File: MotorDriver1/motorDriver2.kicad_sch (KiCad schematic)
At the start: 24 parts, among them Q2 IRLZ44NSTRLPBF, Q3 IRLZ44NSTRLPBF, Q4 IRLZ44NSTRLPBF, Q5 IRLZ44NSTRLPBF

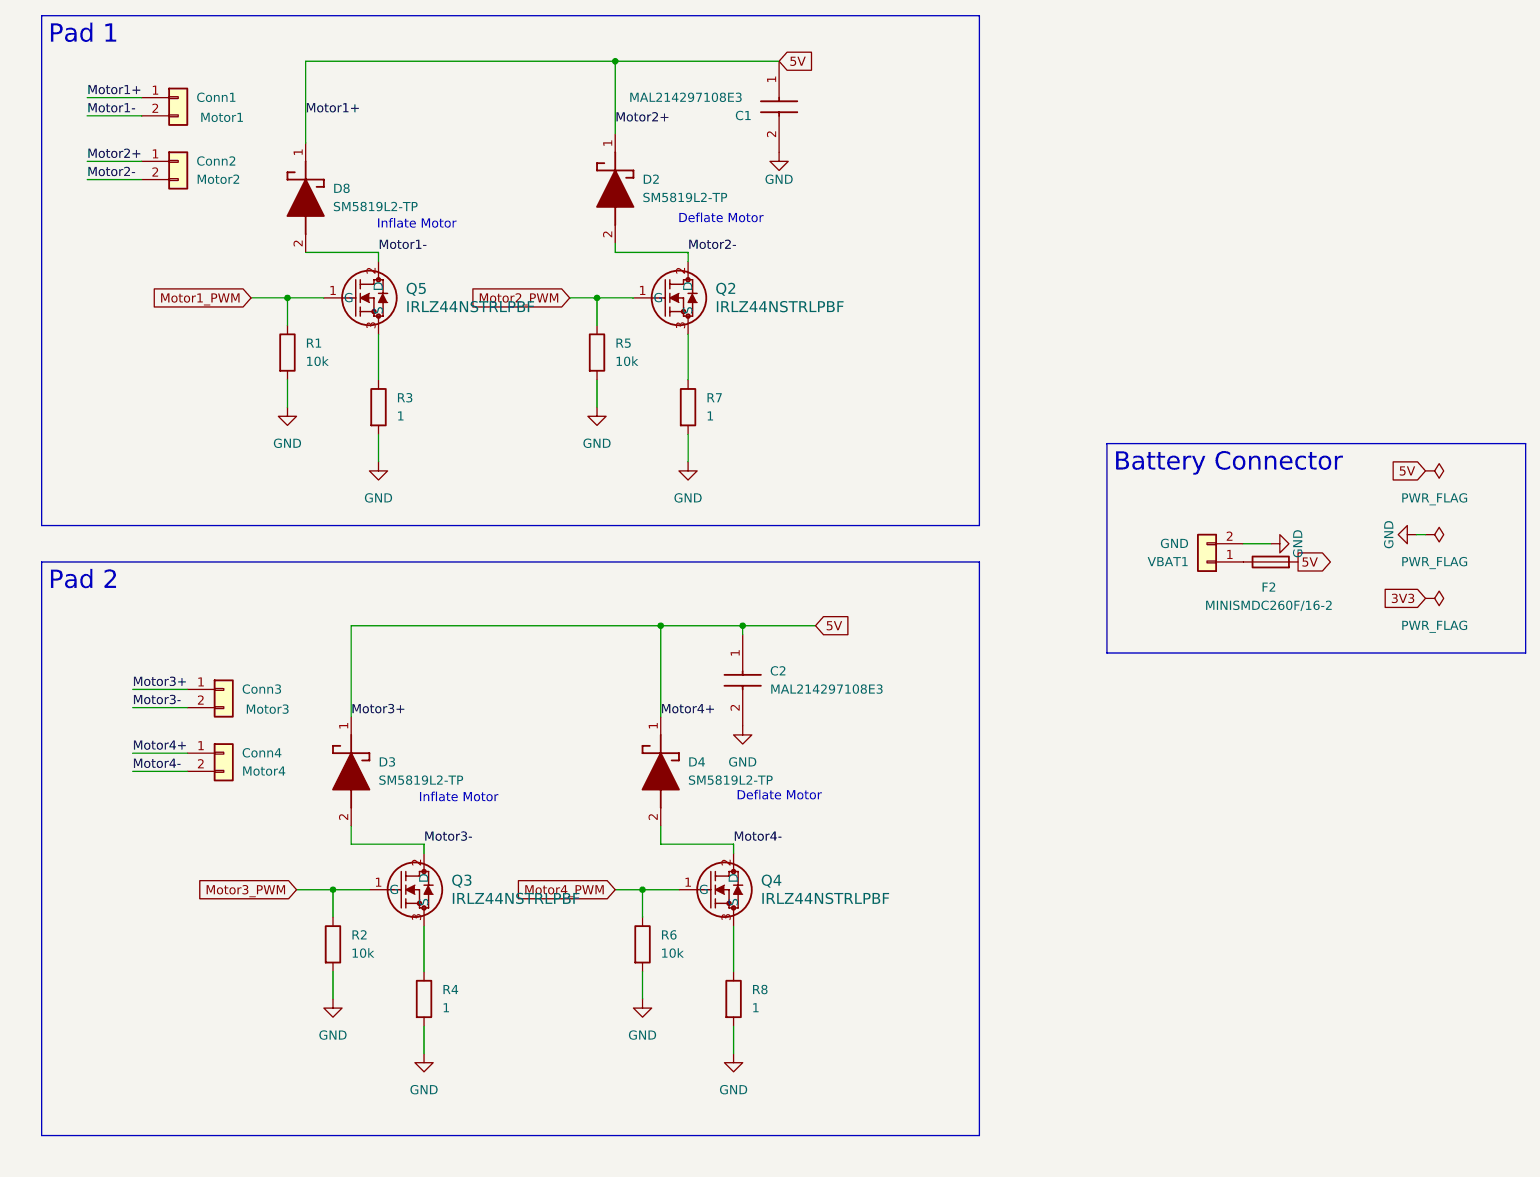
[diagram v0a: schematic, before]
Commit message: added motors and sensors for 4 pad system
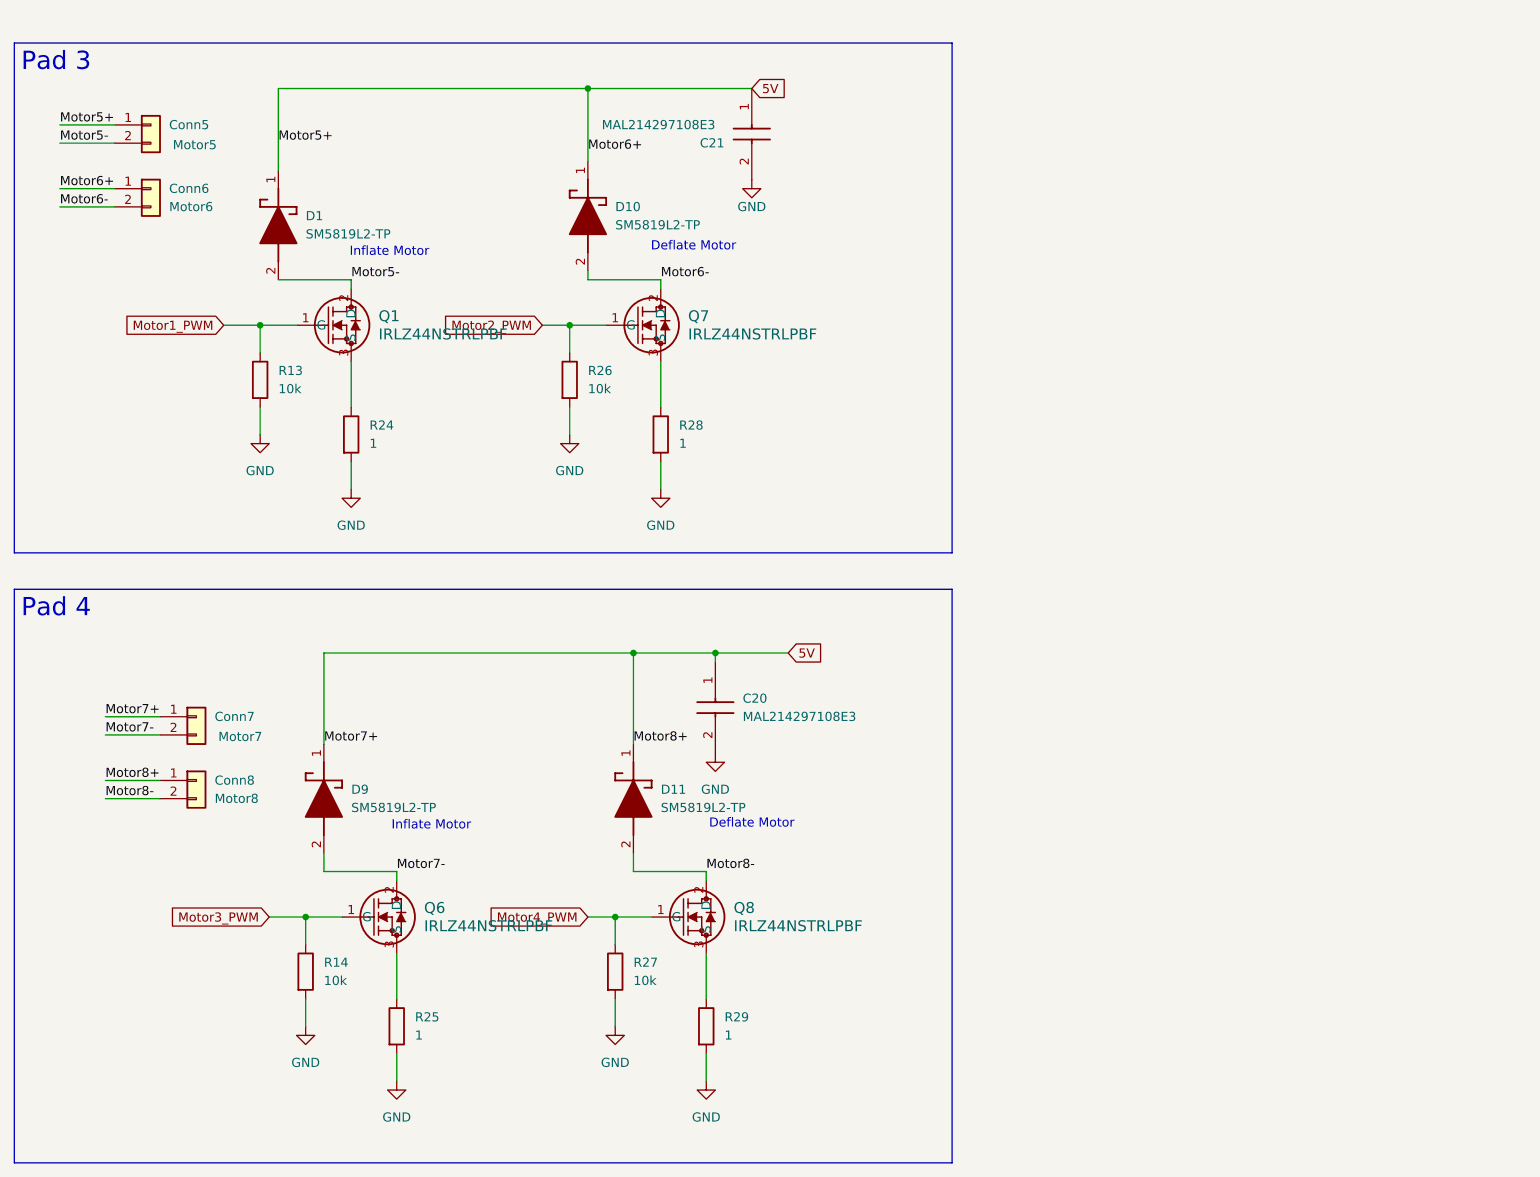
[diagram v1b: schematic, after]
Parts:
- removed C1, C2: MAL214297108E3, footprintLib:CAPAE680X800N, symbol pcb:MAL214297108E3
- removed Conn1: Motor1, Connector_PinHeader_2.54mm:PinHeader_1x02_P2.54mm_Vertical, symbol Connector_Generic:Conn_01x02
- removed Conn2: Motor2, Connector_PinHeader_2.54mm:PinHeader_1x02_P2.54mm_Vertical, symbol Connector_Generic:Conn_01x02
- removed Conn3: Motor3, Connector_PinHeader_2.54mm:PinHeader_1x02_P2.54mm_Vertical, symbol Connector_Generic:Conn_01x02
- removed Conn4: Motor4, Connector_PinHeader_2.54mm:PinHeader_1x02_P2.54mm_Vertical, symbol Connector_Generic:Conn_01x02
- removed D2, D3, D4, D8: SM5819L2-TP, footprintLib:SDO_SM5819L2-TP_MCE, symbol pcb:SM5819L2-TP
- removed F2: MINISMDC260F/16-2, Fuse:Fuse_1812_4532Metric, symbol Device:Fuse
- removed Q2, Q3, Q4, Q5: IRLZ44NSTRLPBF, footprintLib:NMOSGDS_D2PAK_INF, symbol pcb:IRLZ44NSTRLPBF
- removed R1, R2, R5, R6: 10k, Resistor_SMD:R_0402_1005Metric, symbol Device:R
- removed R3, R4, R7, R8: 1, Resistor_SMD:R_1206_3216Metric, symbol Device:R
- removed VBAT1: GND, Connector_PinHeader_2.54mm:PinHeader_1x02_P2.54mm_Vertical, symbol Connector_Generic:Conn_01x02
- added C20, C21: MAL214297108E3, footprintLib:CAPAE680X800N, symbol pcb:MAL214297108E3
- added Conn5: Motor5, Connector_PinHeader_2.54mm:PinHeader_1x02_P2.54mm_Vertical, symbol Connector_Generic:Conn_01x02
- added Conn6: Motor6, Connector_PinHeader_2.54mm:PinHeader_1x02_P2.54mm_Vertical, symbol Connector_Generic:Conn_01x02
- added Conn7: Motor7, Connector_PinHeader_2.54mm:PinHeader_1x02_P2.54mm_Vertical, symbol Connector_Generic:Conn_01x02
- added Conn8: Motor8, Connector_PinHeader_2.54mm:PinHeader_1x02_P2.54mm_Vertical, symbol Connector_Generic:Conn_01x02
- added D1, D10, D11, D9: SM5819L2-TP, footprintLib:SDO_SM5819L2-TP_MCE, symbol pcb:SM5819L2-TP
- added Q1, Q6, Q7, Q8: IRLZ44NSTRLPBF, footprintLib:NMOSGDS_D2PAK_INF, symbol pcb:IRLZ44NSTRLPBF
- added R13, R14, R26, R27: 10k, Resistor_SMD:R_0402_1005Metric, symbol Device:R
- added R24, R25, R28, R29: 1, Resistor_SMD:R_1206_3216Metric, symbol Device:R
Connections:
- net 5V: now also C20.1 (+), C21.1 (+), Conn5.1 (Pin_1), Conn6.1 (Pin_1), Conn7.1 (Pin_1), Conn8.1 (Pin_1), D1.1 (K), D10.1 (K), D11.1 (K), D9.1 (K)
- net GND: now also C20.2 (-), C21.2 (-), R13.2, R14.2, R24.2, R25.2, R26.2, R27.2, R28.2, R29.2
- net Motor1_PWM: now also Q1.1 (G), R13.1
- net Motor2_PWM: now also Q7.1 (G), R26.1
- net Motor3_PWM: now also Q6.1 (G), R14.1
- net Motor4_PWM: now also Q8.1 (G), R27.1
- new net: Q6.3 (S), R25.1
- new net: Q1.3 (S), R24.1
- new net: Q8.3 (S), R29.1
- new net: Q7.3 (S), R28.1
- new net Motor5-: Conn5.2 (Pin_2), D1.2 (A), Q1.2 (D)
- new net Motor6-: Conn6.2 (Pin_2), D10.2 (A), Q7.2 (D)
- new net Motor7-: Conn7.2 (Pin_2), D9.2 (A), Q6.2 (D)
- new net Motor8-: Conn8.2 (Pin_2), D11.2 (A), Q8.2 (D)
